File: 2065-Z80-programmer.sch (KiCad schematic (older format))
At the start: 29 parts, among them J1 Conn_01x05, J2 Conn_02x20_Counter_Clockwise, J3 Conn_01x02, J4 Conn_02x20_Odd_Even, Q1 2N7000, Q2 2N7000, Q3 PN2222, U1 MCP23017-E_SP, U2 MCP23017-E_SP

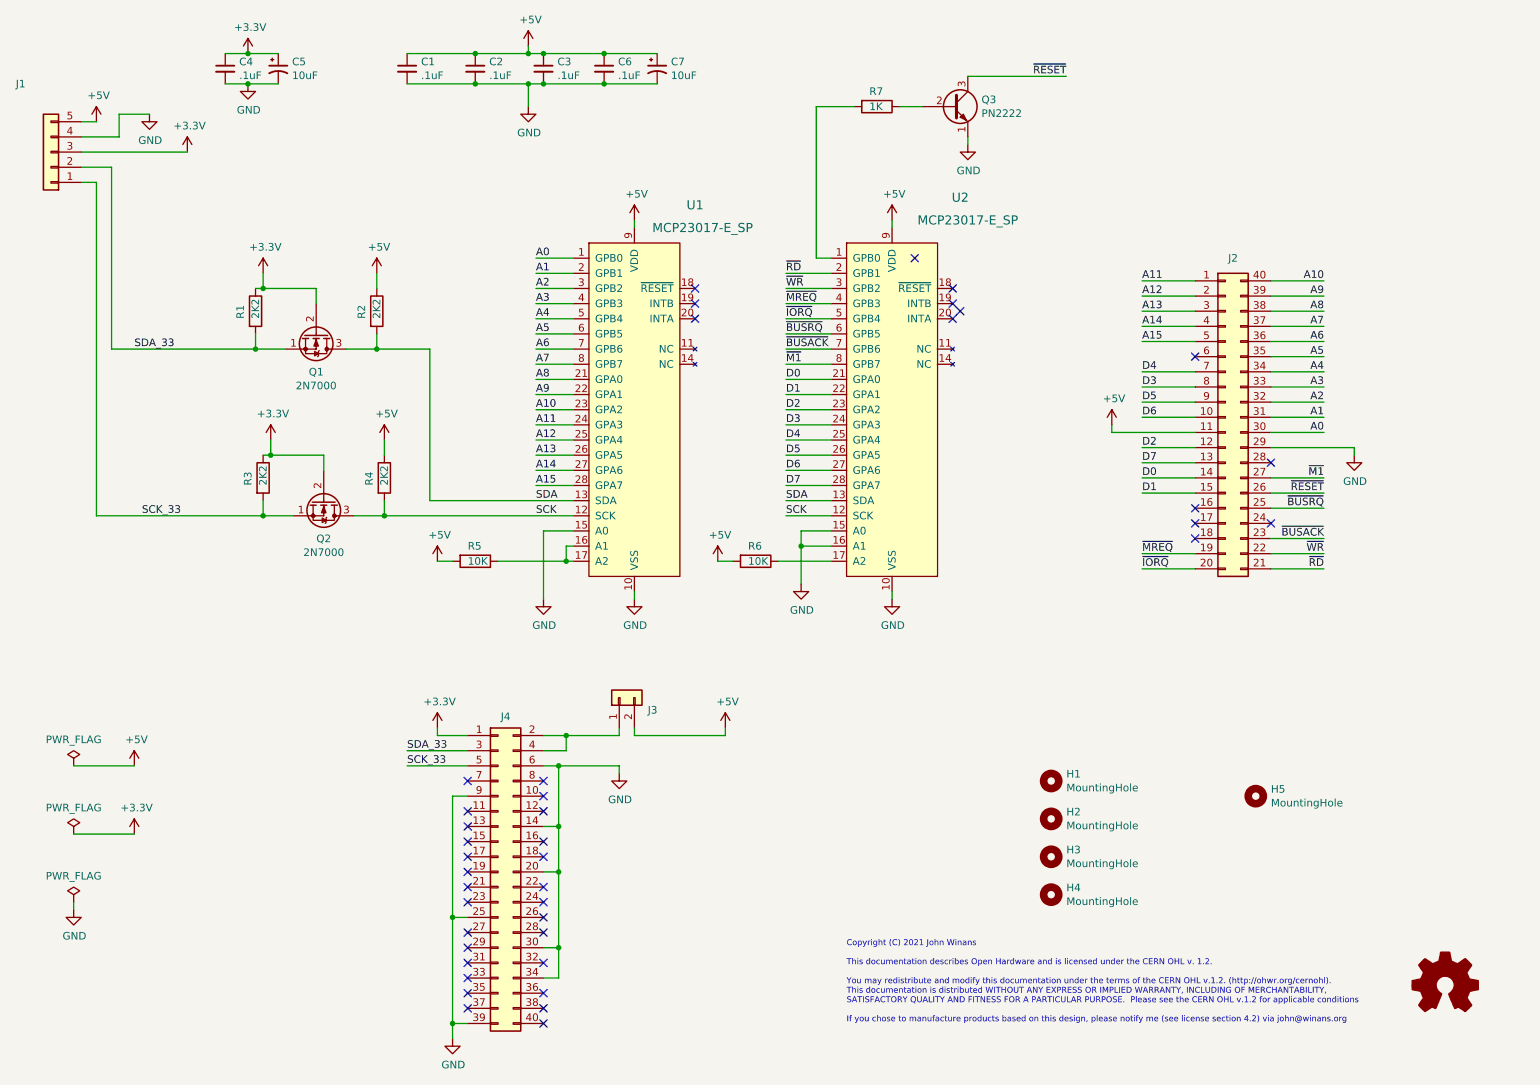
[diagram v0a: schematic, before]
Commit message: Pull up /RESET
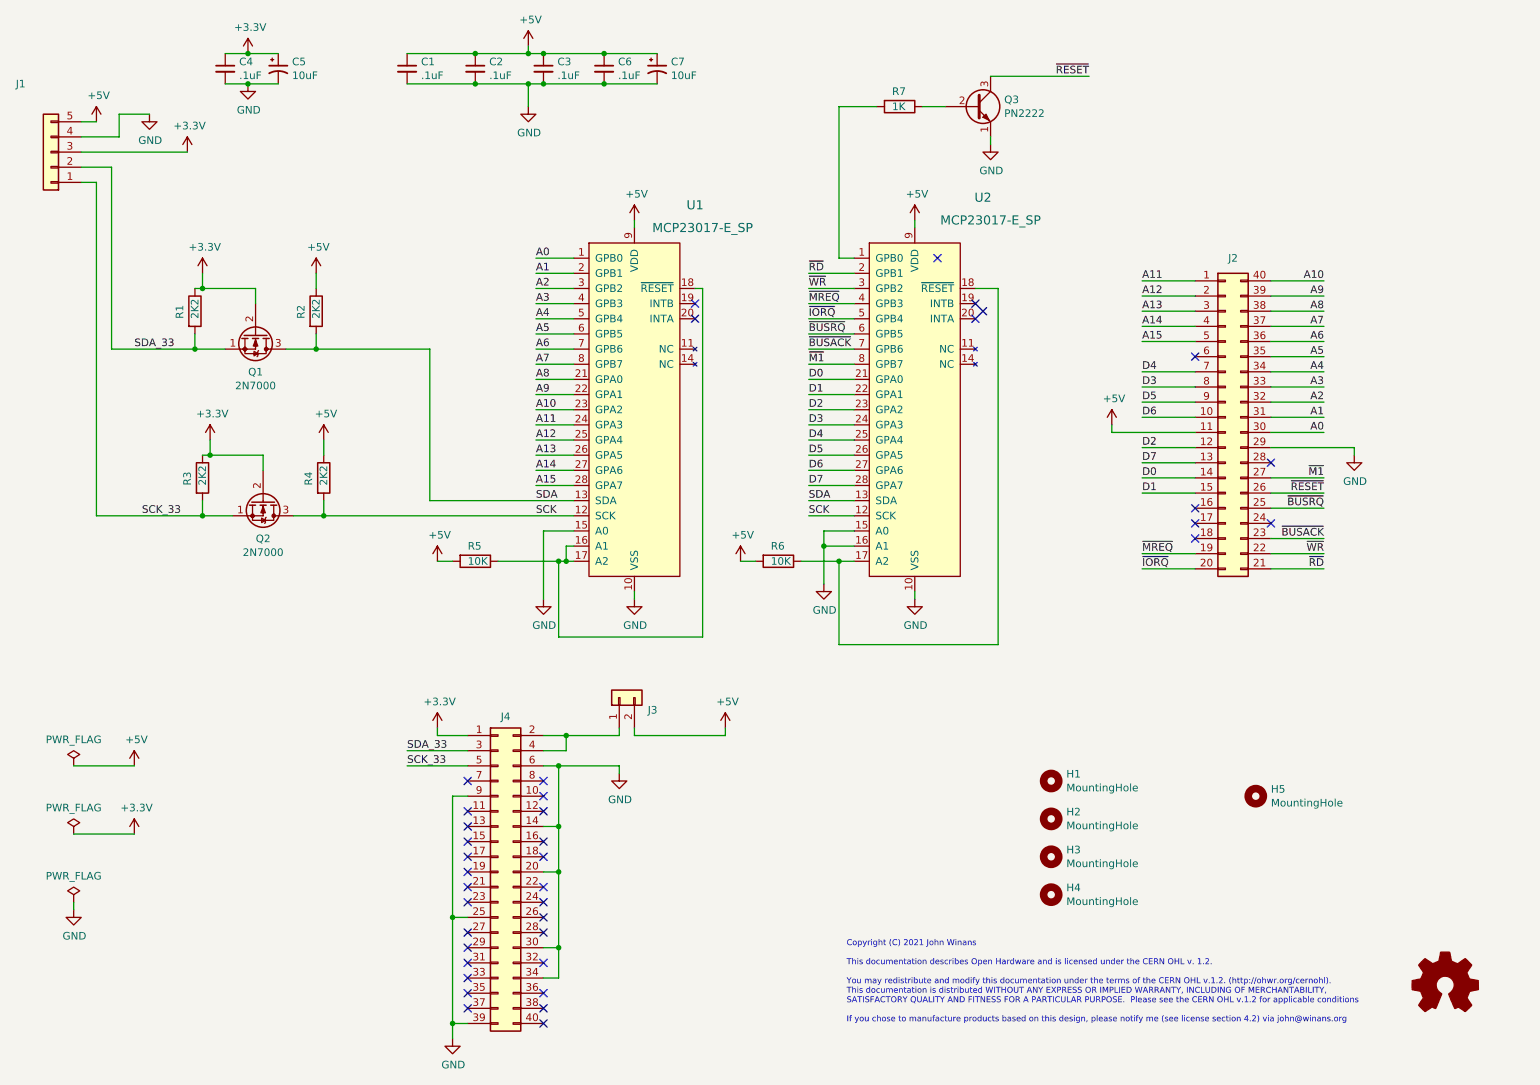
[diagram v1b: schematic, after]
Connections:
- net at R5.1, U1.16 (A1), U1.17 (A2): now also U1.18 (~RESET)
- net at R6.1, U2.17 (A2): now also U2.18 (~RESET)
- no-connect marks 41 -> 39
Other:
- moved on the sheet: Q1, Q2, Q3, R1, R2, R3, R4, R6, R7, U2

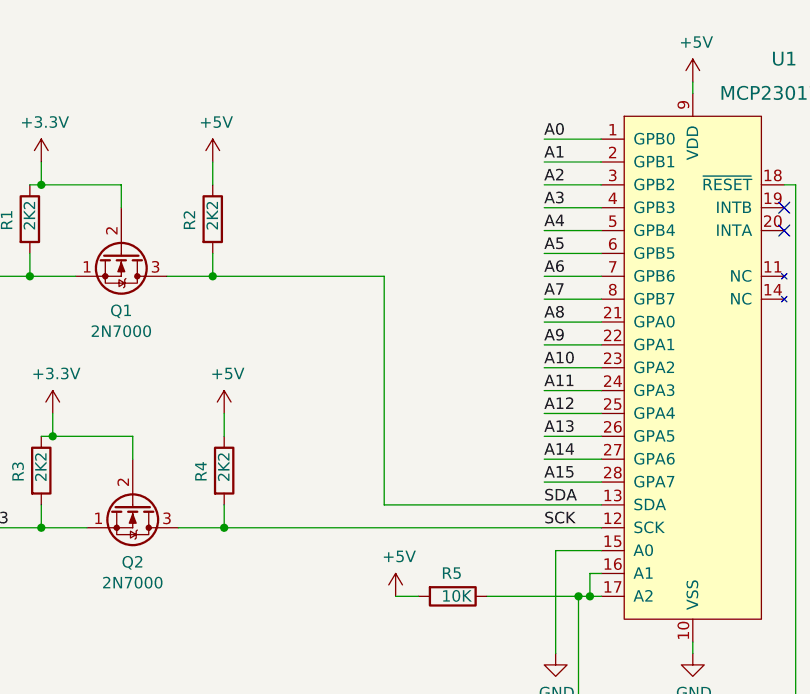
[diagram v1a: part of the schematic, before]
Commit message: Add 5V clamping diodes to I2C lines Move mounting hole clear of user-1 header
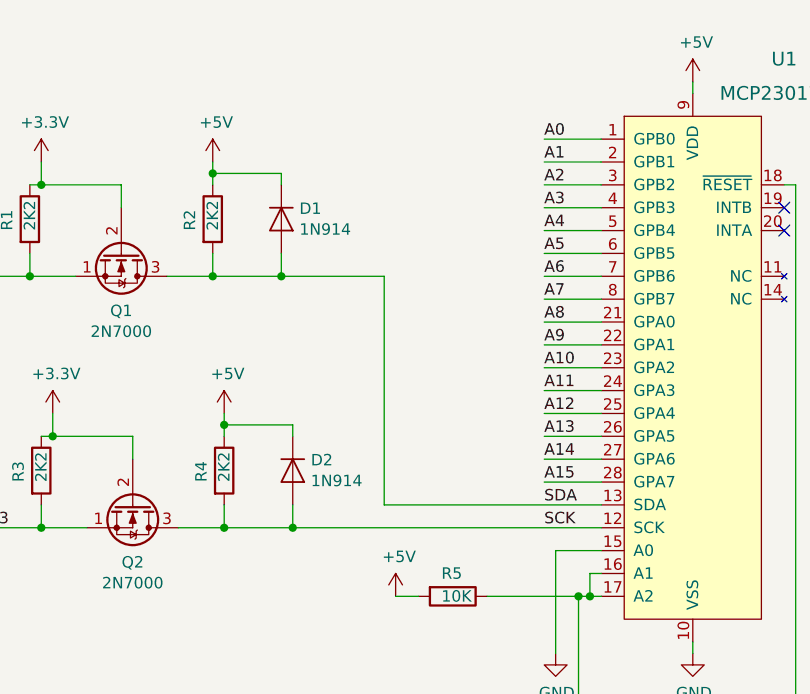
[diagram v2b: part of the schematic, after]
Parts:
- added D1, D2: 1N914, Diode_THT:D_DO-35_SOD27_P7.62mm_Horizontal, symbol Device:D
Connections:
- net +5V: now also D1.1 (K), D2.1 (K)
- net SCK: now also D2.2 (A)
- net SDA: now also D1.2 (A)
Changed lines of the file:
@@
 $EndComp
 Wire Wire Line
-	2850 3500 2850 3600
+	2850 3500 2850 3550
 $Comp
 L JWlib:2N7000 Q1
@@
 Connection ~ 2800 2900
 Wire Wire Line
-	2800 2900 3550 2900
+	2800 2900 3100 2900
 $Comp
 L power:+5V #PWR05
@@
 $EndComp
 Wire Wire Line
-	2800 2400 2800 2500
-Wire Wire Line
-	2850 4000 4500 4000
+	2800 2400 2800 2450
+Wire Wire Line
+	2850 4000 3150 4000
 Wire Wire Line
 	4500 3900 3550 3900
@@
 Wire Wire Line
 	4400 4300 4000 4300
+$Comp
+L Device:D D1
+U 1 1 618EEB95
+P 3100 2650
+F 0 "D1" V 3054 2729 50  0000 L CNN
+F 1 "1N914" V 3145 2729 50  0000 L CNN
+F 2 "Diode_THT:D_DO-35_SOD27_P7.62mm_Horizontal" H 3100 2650 50  0001 C CNN
+F 3 "http://www.vishay.com/docs/85622/1n914.pdf" H 3100 2650 50  0001 C CNN
+F 4 "1N4148FSCT-ND" H 3100 2650 50  0001 C CNN "Digi-Key_PN"
+F 5 "1N4148TR" H 3100 2650 50  0001 C CNN "MPN"
+F 6 "onsemi" H 3100 2650 50  0001 C CNN "Manufacturer"
+	1    3100 2650
+	0    1    1    0
+$EndComp
+Connection ~ 3100 2900
+Wire Wire Line
+	3100 2900 3550 2900
+Wire Wire Line
+	3100 2800 3100 2900
+Wire Wire Line
+	3100 2500 3100 2450
+Wire Wire Line
+	3100 2450 2800 2450
+Connection ~ 2800 2450
+Wire Wire Line
+	2800 2450 2800 2500
+$Comp
+L Device:D D2
+U 1 1 6190C4CE
+P 3150 3750
+F 0 "D2" V 3104 3829 50  0000 L CNN
+F 1 "1N914" V 3195 3829 50  0000 L CNN
+F 2 "Diode_THT:D_DO-35_SOD27_P7.62mm_Horizontal" H 3150 3750 50  0001 C CNN
+F 3 "http://www.vishay.com/docs/85622/1n914.pdf" H 3150 3750 50  0001 C CNN
+F 4 "1N4148FSCT-ND" H 3150 3750 50  0001 C CNN "Digi-Key_PN"
+F 5 "1N4148TR" H 3150 3750 50  0001 C CNN "MPN"
+F 6 "onsemi" H 3150 3750 50  0001 C CNN "Manufacturer"
+	1    3150 3750
+	0    1    1    0
+$EndComp
+Wire Wire Line
+	3150 3900 3150 4000
+Wire Wire Line
+	3150 3600 3150 3550
+Wire Wire Line
+	3150 3550 2850 3550
+Connection ~ 3150 4000
+Wire Wire Line
+	3150 4000 4500 4000
+Connection ~ 2850 3550
+Wire Wire Line
+	2850 3550 2850 3600
 $EndSCHEMATC

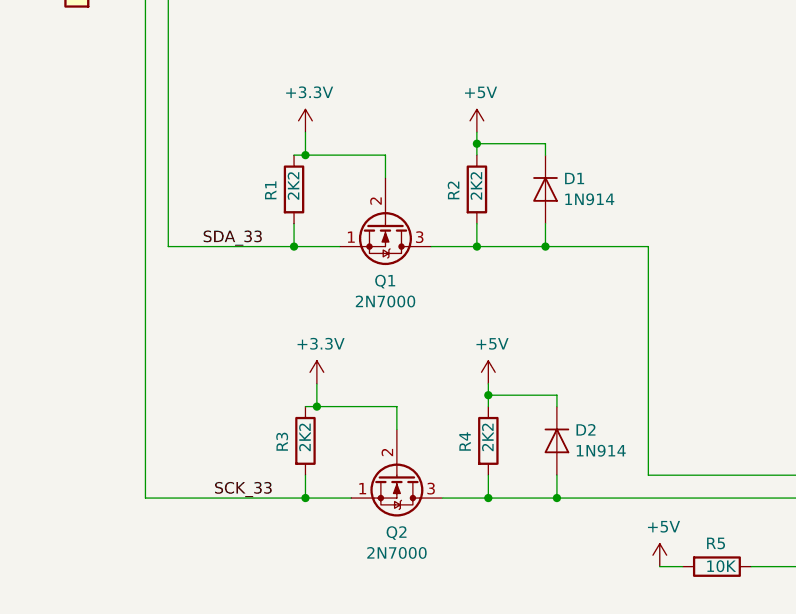
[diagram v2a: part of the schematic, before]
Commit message: Update sch, pcb, & BOM to match as-built v1.0.
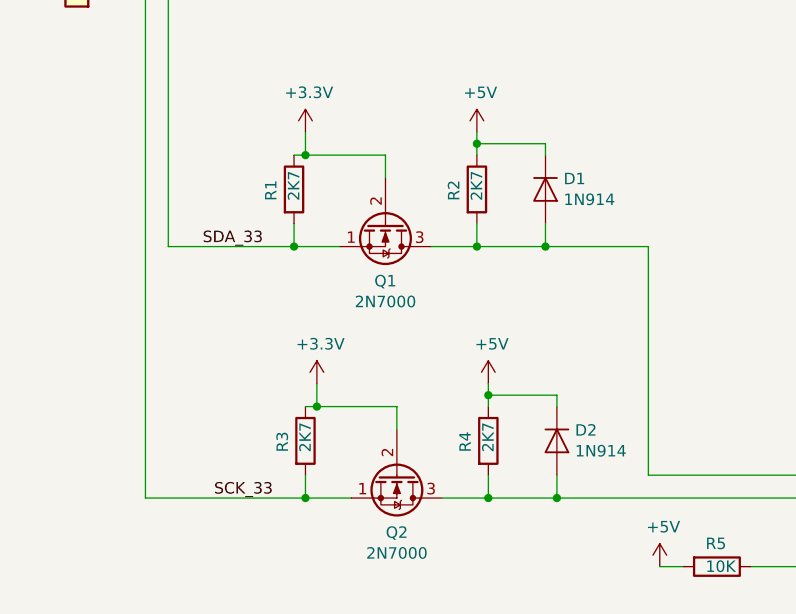
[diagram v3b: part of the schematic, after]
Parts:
- C1, C2, C3, C4, C6: Description (none) -> CAP CER 0.1UF 50V Z5U RADIAL; Digi-Key_PN (none) -> 399-9859-1-ND‎
- C5, C7: Description (none) -> CAP ALUM 10UF 20% 25V RADIAL; Digi-Key_PN (none) -> P975-ND; MPN (none) -> ECE-A1EKS100
- D1, D2: Description (none) -> 100V 0.3A Small Signal Fast Switching Diode, DO-35
- J1: Description (none) -> Generic connector, single row, 01x05; Digi-Key_PN (none) -> S1211EC-05-ND
- J2, J4: Description (none) -> Generic connector, double row, 02x20; Digi-Key_PN (none) -> S2011EC-20-ND
- J3: Description (none) -> Generic connector, single row, 01x02; Digi-Key_PN (none) -> S1011EC-02-ND
- Q1, Q2: Description (none) -> MOSFET N-CH 60V 200MA TO92-3; Digi-Key_PN (none) -> 2N7000TACT-ND; MPN (none) -> 2N7000TA; Manufacturer (none) -> onsemi
- Q3: Description (none) -> NPN transistor; Digi-Key_PN (none) -> 1514-PN2222APBFREE-ND
- R1, R2, R3, R4: value 2K2 -> 2K7; Description (none) -> RES 2.7K OHM 5% 1/8W AXIAL; Digi-Key_PN (none) -> CF18JT2K70CT-ND; MPN (none) -> CF18JT2K70; Manufacturer (none) -> Stackpole Electronics Inc
- R5, R6: Description (none) -> RES 10K OHM 5% 1/8W AXIAL; Digi-Key_PN (none) -> CF18JT10K0CT-ND; MPN (none) -> CF18JT10K0; Manufacturer (none) -> Stackpole Electronics Inc
- R7: Description (none) -> RES 1K OHM 5% 1/8W AXIAL; Digi-Key_PN (none) -> CF18JT1K00CT-ND; MPN (none) -> CF18JT1K00; Manufacturer (none) -> Stackpole Electronics Inc

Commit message: Correct J2 to female connector.
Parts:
- J2: Description Generic connector, double row, 02x20 -> Female connector, double row, 02x20; Digi-Key_PN S2011EC-20-ND -> S6104-ND; MPN (none) -> PPTC202LFBN-RC; Manufacturer (none) -> Sullins Connector Solutions
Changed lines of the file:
@@
 F 1 "Conn_02x20_Counter_Clockwise" H 8850 4376 50  0001 C CNN
 F 2 "jb-footprint:PinHeader_2x20_P2.54mm_Vertical_counterclock" H 8800 3350 50  0001 C CNN
-F 3 "https://drawings-pdf.s3.amazonaws.com/11636.pdf" H 8800 3350 50  0001 C CNN
-F 4 "Generic connector, double row, 02x20" H 8800 3350 50  0001 C CNN "Description"
-F 5 "S2011EC-20-ND" H 8800 3350 50  0001 C CNN "Digi-Key_PN"
+F 3 "https://media.digikey.com/pdf/Data%20Sheets/Sullins%20PDFs/Female_Headers.100_DS.pdf" H 8800 3350 50  0001 C CNN
+F 4 "Female connector, double row, 02x20" H 8800 3350 50  0001 C CNN "Description"
+F 5 "S6104-ND" H 8800 3350 50  0001 C CNN "Digi-Key_PN"
+F 6 "PPTC202LFBN-RC" H 8800 3350 50  0001 C CNN "MPN"
+F 7 "Sullins Connector Solutions" H 8800 3350 50  0001 C CNN "Manufacturer"
 	1    8800 3350
 	1    0    0    -1

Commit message: Change Z80 header to socket so looks right in 3D
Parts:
- J2: footprint jb-footprint:PinHeader_2x20_P2.54mm_Vertical_counterclock -> jb-footprint:PinSocket_2x20_P2.54mm_Vertical_clockwise
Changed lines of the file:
@@
 F 0 "J2" H 8850 4400 50  0000 C CNN
 F 1 "Conn_02x20_Counter_Clockwise" H 8850 4376 50  0001 C CNN
-F 2 "jb-footprint:PinHeader_2x20_P2.54mm_Vertical_counterclock" H 8800 3350 50  0001 C CNN
+F 2 "jb-footprint:PinSocket_2x20_P2.54mm_Vertical_clockwise" H 8800 3350 50  0001 C CNN
 F 3 "https://media.digikey.com/pdf/Data%20Sheets/Sullins%20PDFs/Female_Headers.100_DS.pdf" H 8800 3350 50  0001 C CNN
 F 4 "Female connector, double row, 02x20" H 8800 3350 50  0001 C CNN "Description"
